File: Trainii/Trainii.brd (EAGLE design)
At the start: 50.8 x 71.1 mm, 32 parts, among them J1 APDS-9960, J2 Left Motor Encoder, J3 Right Motor Encoder, J4 Line Sensor 1, J5 Line Sensor 2, J6 Ultrasonic, J7 Left Motor Output, J8 Right Motor Output, J9 Lift Motor Output, U1 TPS61222DCKR, U2 BSS138

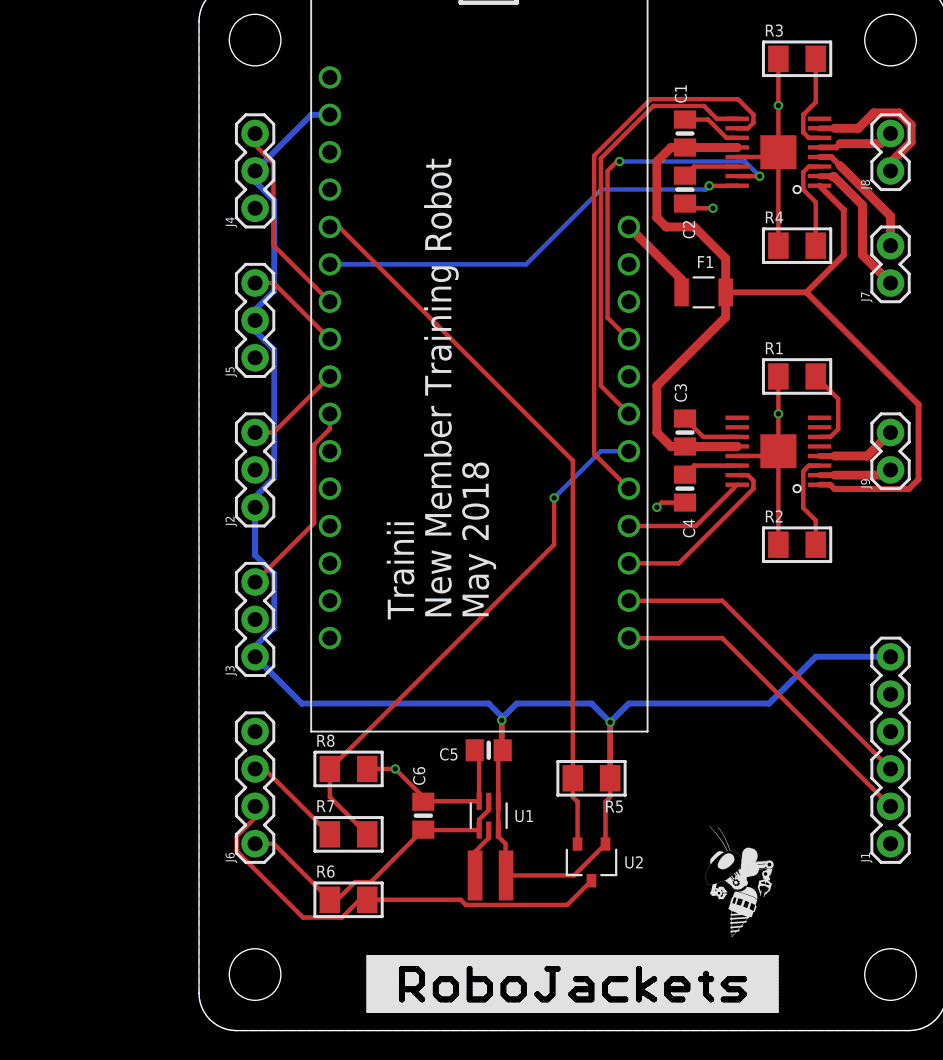
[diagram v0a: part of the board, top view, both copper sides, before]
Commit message: Updated Library, began fixing schematic
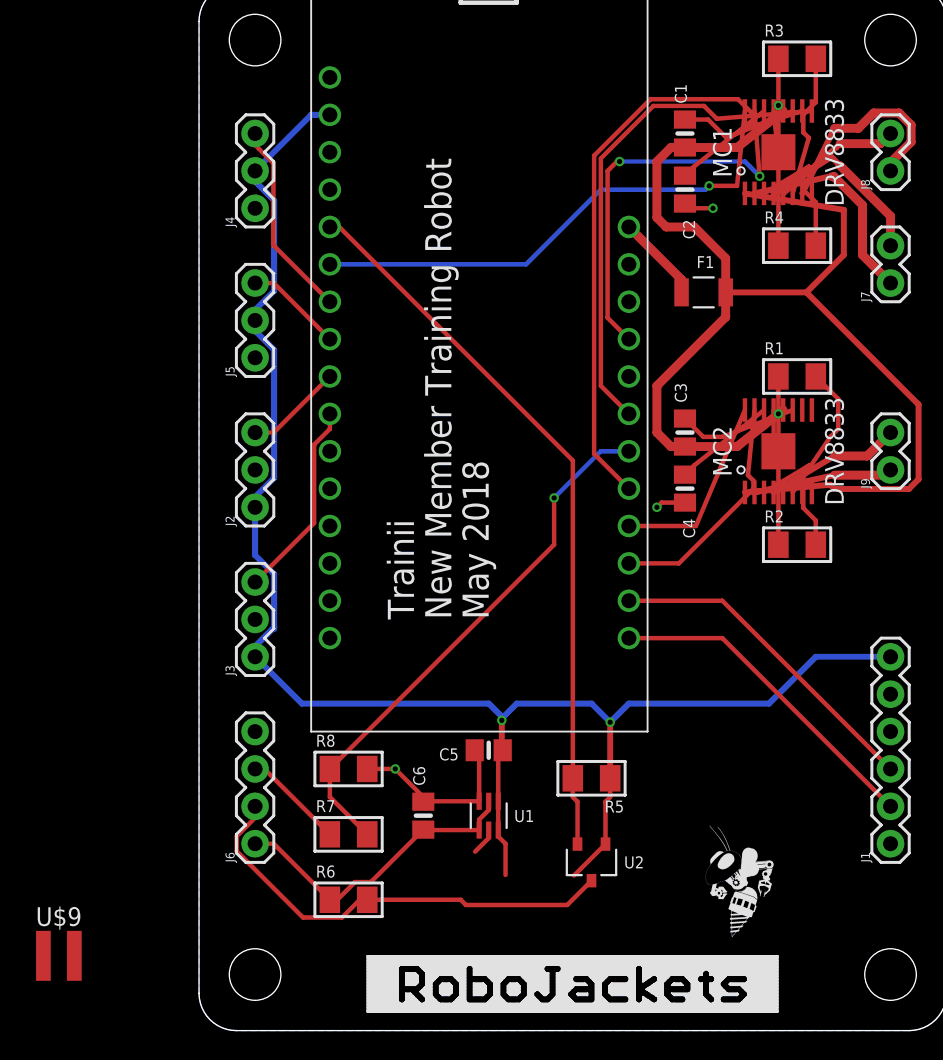
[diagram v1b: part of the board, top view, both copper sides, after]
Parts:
- removed U$12: VLS3012HBX, Trainii:VLS3012HBX
- added U$9: VLS3012HBX, Trainii:VLS3012HBX
- MC1, MC2: device Trainii:DRV8833 -> Trainii:HTSSOP-16
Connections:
- net 3V: now also U$9.1; no longer U$12.P$2
- net GND: now also MC1.13, MC1.17, MC2.13, MC2.17; no longer MC1.GND, MC1.GNDP, MC2.GND, MC2.GNDP
- net LEFT_0: now also MC1.2; no longer MC1.AOUT1
- net LEFT_1: now also MC1.4; no longer MC1.AOUT2
- net LEFT_A: now also MC1.16; no longer MC1.AIN1
- net LEFT_B: now also MC1.15; no longer MC1.AIN2
- net LIFT_0: now also MC2.2; no longer MC2.AOUT1
- net LIFT_1: now also MC2.4; no longer MC2.AOUT2
- net LIFT_A: now also MC2.16; no longer MC2.AIN1
- net LIFT_B: now also MC2.15; no longer MC2.AIN2
- net N$1: now also U$9.2; no longer U$12.P$1
- net N$10: now also MC1.3; no longer MC1.AISEN
- net N$3: now also MC2.11; no longer MC2.VCP
- net N$4: now also MC2.6; no longer MC2.BISEN
- net N$5: now also MC2.14; no longer MC2.VINT
- net N$6: now also MC2.3; no longer MC2.AISEN
- net N$7: now also MC1.11; no longer MC1.VCP
- net N$8: now also MC1.14; no longer MC1.VINT
- net N$9: now also MC1.6; no longer MC1.BISEN
- net RIGHT_0: now also MC1.7; no longer MC1.BOUT1
- net RIGHT_1: now also MC1.5; no longer MC1.BOUT2
- net RIGHT_A: now also MC1.9; no longer MC1.BIN1
- net RIGHT_B: now also MC1.10; no longer MC1.BIN2
- net VBAT_FUSE: now also MC1.1, MC1.12, MC2.1, MC2.12; no longer MC1.NSLEEP, MC1.VM, MC2.NSLEEP, MC2.VM
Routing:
- net VBAT_FUSE: track 72.6 -> 90.1 mm
- net LEFT_A: track 29.9 -> 35.0 mm
- net RIGHT_A: track 29.2 -> 34.3 mm
- net 3V: track 118.1 -> 113.4 mm
- net LIFT_A: track 8.52 -> 13.1 mm
- net LEFT_0: track 9.82 -> 14.4 mm
- net LIFT_0: track 4.97 -> 9.52 mm
- net N$7: track 4.07 -> 8.20 mm
- net N$3: track 4.07 -> 8.18 mm
- net RIGHT_0: track 10.7 -> 14.6 mm
- net LEFT_1: track 8.49 -> 12.3 mm
- net N$4: track 5.69 -> 9.52 mm
- net LIFT_1: track 5.48 -> 9.29 mm
- net LIFT_B: track 12.4 -> 16.1 mm
- net RIGHT_1: track 5.21 -> 8.85 mm
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
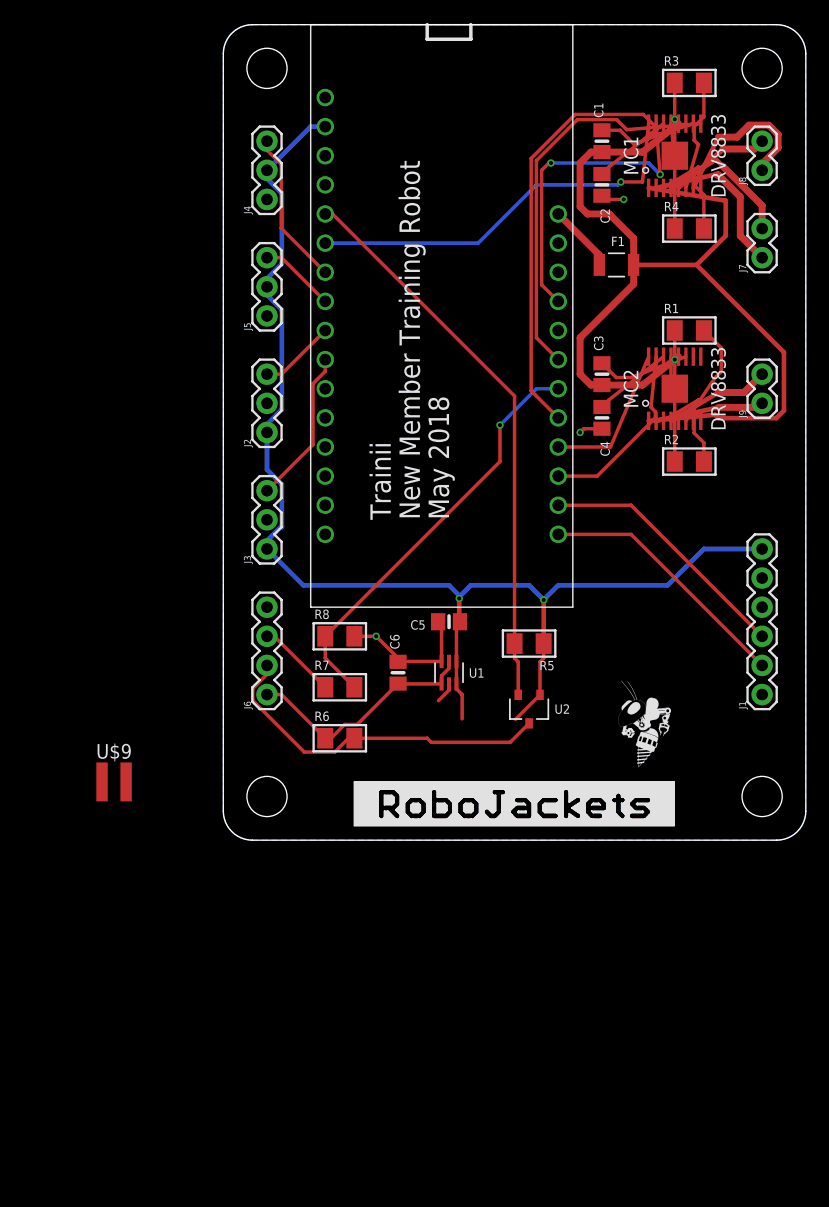
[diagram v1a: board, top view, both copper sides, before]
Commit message: Continued library update and finished schematic driver correction
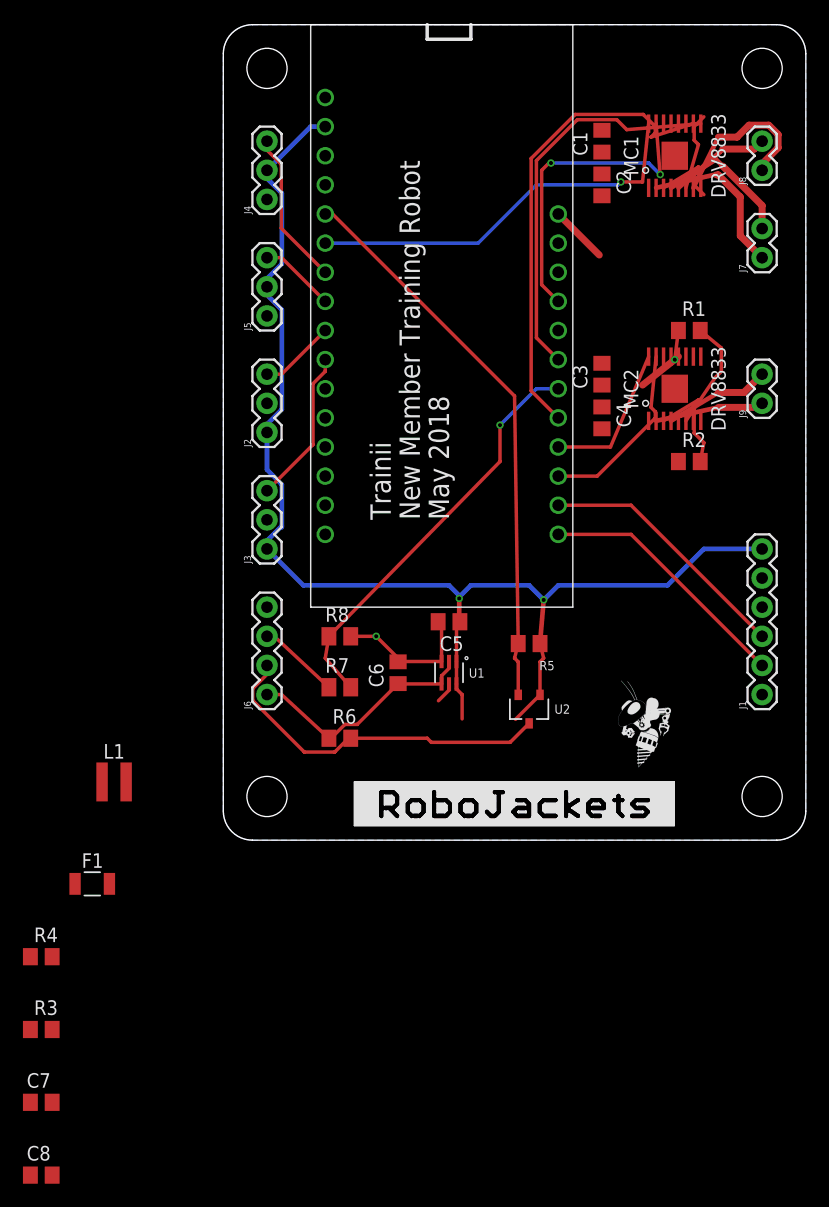
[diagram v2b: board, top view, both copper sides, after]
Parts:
- added C7, C8: 2.2uF, rcl:C0805
- C1, C3: value 0.1uF -> 0.01uF; device microbuilder:0805-NO -> rcl:C0805
- C2, C4: value 10µF -> 10uF; device microbuilder:0805-NO -> rcl:C0805
- C5: value 10uF -> 10uF 6.3V; device microbuilder:0805-NO -> rcl:C0805
- C6: value 10uF -> 10uF 16V; device microbuilder:0805-NO -> rcl:C0805
- F1: device Trainii:0ZCJ -> Trainii:1206
- L1: value VLS3012HBX -> 4.7 uH
- R1, R2, R5, R6: device microbuilder:_1206 -> rcl:R0805
- R3, R4: value 0.2Ω -> 0.2 Ohm; device microbuilder:_1206 -> rcl:R0805
- R7, R8: device microbuilder:_1206 -> rcl:M0805
- moved R3 100.0 mm to (-15.9, -16.5)
- moved R4 85.0 mm to (-15.9, -10.2)
- moved F1 70.7 mm to (-11.4, -3.81)
- renumbered U$9 to L1
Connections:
- removed net N$3: C3.2, MC2.11
- new net MOTOR_FAULT: MC1.8, MC2.8, U$6.21
- new net N$11: C3.1, MC2.11
- new net N$2: R1.1, R2.1
- net GND: now also C7.2, C8.2, R3.2, R4.2; no longer R1.1, R2.1, R3.1, R4.1
- net N$10: now also R4.1; no longer R4.2
- net N$5: now also C8.1; no longer C4.1
- net N$7: now also C1.1; no longer C1.2
- net N$8: now also C7.1; no longer C2.1
- net N$9: now also R3.1; no longer R3.2
- net VBAT_FUSE: now also C1.2, C2.1, C3.2, C4.1; no longer C1.1, C3.1, F1.2
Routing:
- net VBAT_FUSE: track 90.1 -> 3.99 mm
- net GND: track 47.6 -> 12.6 mm, vias 5 -> 1
- net N$7: track 8.20 -> 0.00 mm
- net N$3: track 8.18 -> 0.00 mm
- net N$8: track 6.94 -> 0.00 mm
- net N$5: track 6.94 -> 0.00 mm
- net N$9: track 9.81 -> 6.86 mm
- net N$10: track 9.43 -> 6.47 mm
- net N$2: track 0.00 -> 2.56 mm, vias 0 -> 1
- net VBAT: track 5.93 -> 5.06 mm

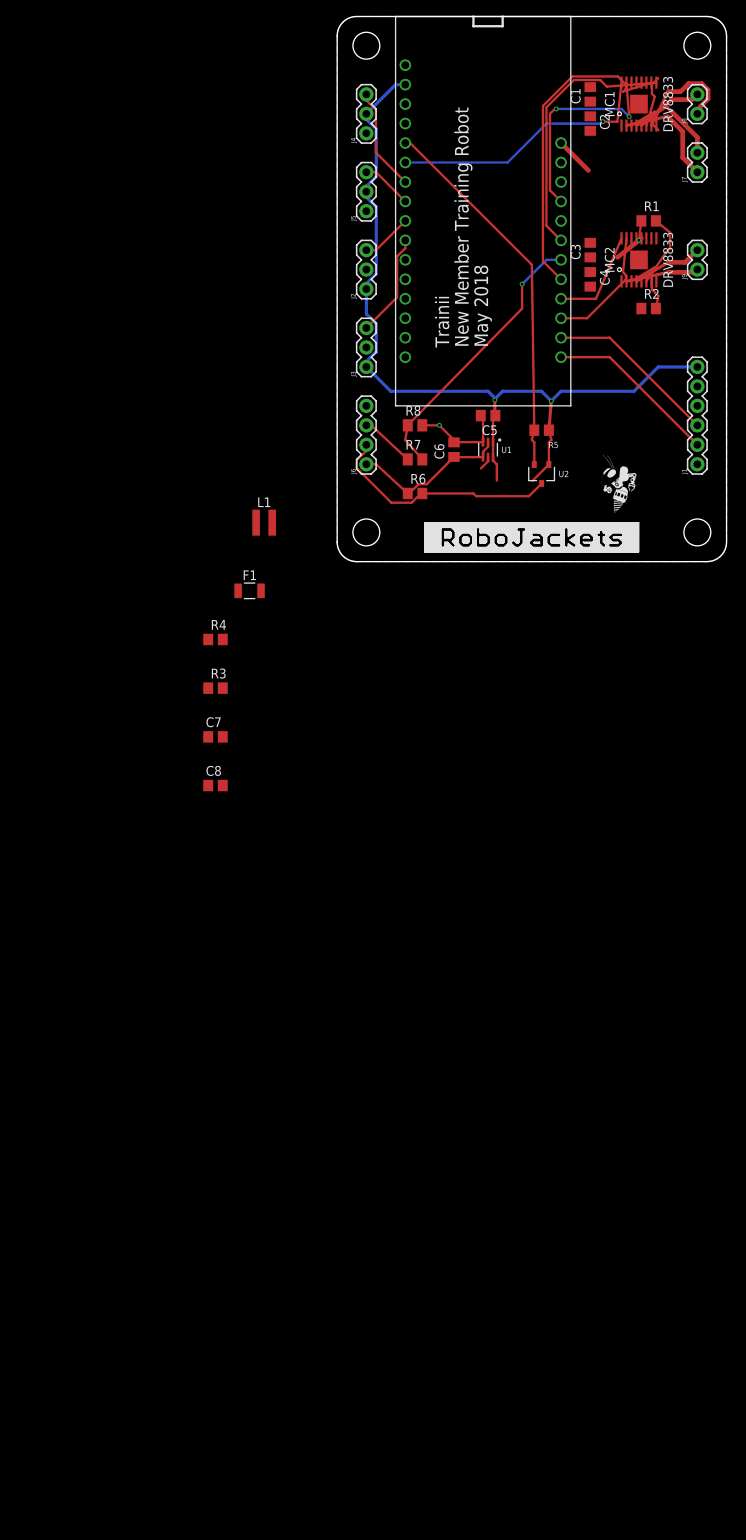
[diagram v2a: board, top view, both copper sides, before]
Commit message: Added new battery connector
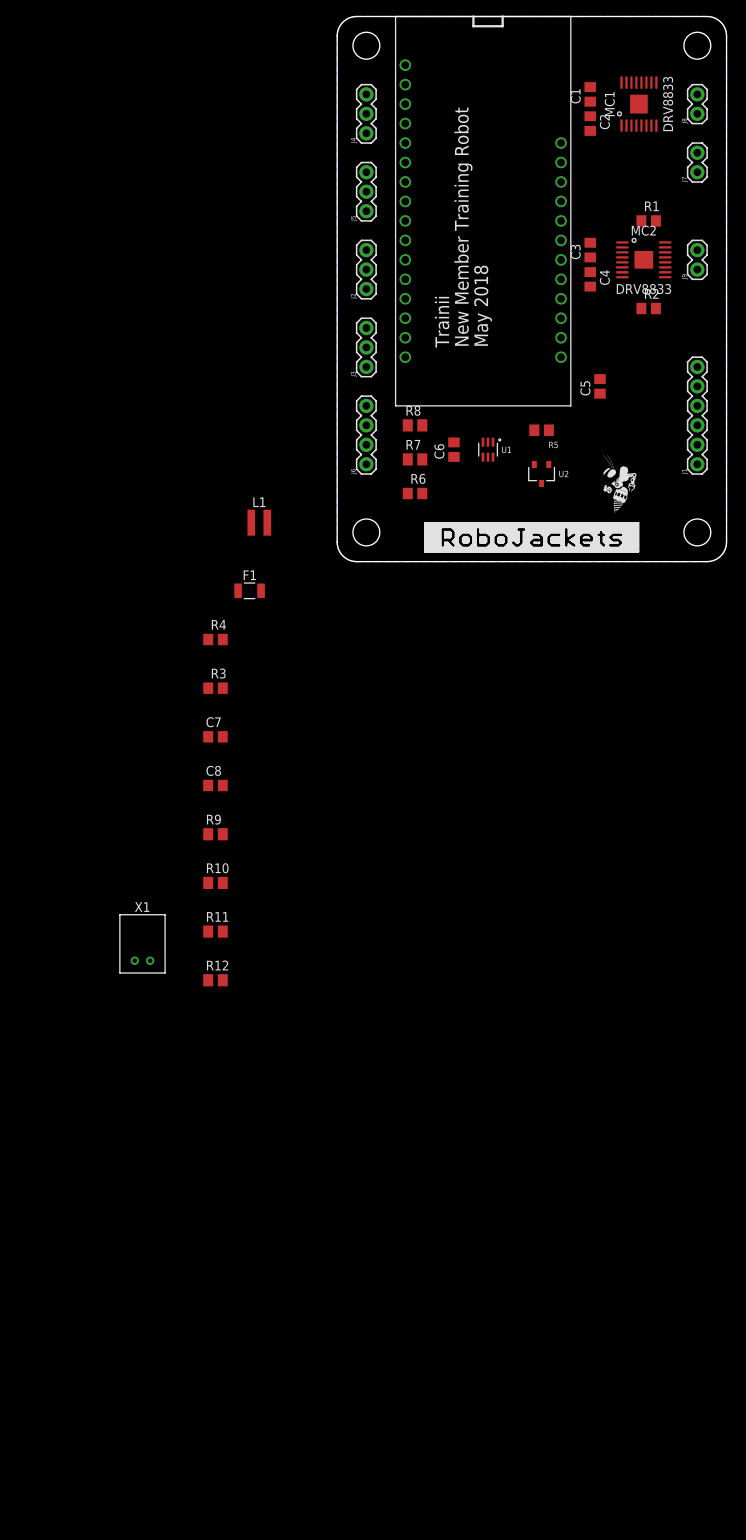
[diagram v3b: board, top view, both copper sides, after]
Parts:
- added R10, R12: 91Ω, rcl:M0805
- added R11, R9: 47Ω, rcl:M0805
- added X1: JST-PH2, Trainii:JST-PH
- moved C5 15.1 mm to (34.3, 22.9), turned to 90 degrees
- moved MC2 0.64 mm to (40.0, 39.4), turned to 0 degrees
- moved L1 0.63 mm to (-10.2, 5.08)
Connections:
- net ECHO renamed ECHO_5V
- net ECHO3.3 renamed ECHO_3V3
- net TRIG renamed TRIG_5V
- net TRIG3.3 renamed TRIG_3V3
- removed net 3V: C5.1, J1.6, J2.1, J3.1, J4.2, J5.2, L1.1, R5.1, U$6.3V, U1.1, U1.6, U2.1
- new net 3V3: C5.1, J1.6, J2.1, J3.1, L1.1, R5.1, U$6.3V, U1.1, U1.6, U2.1
- new net LINE_OUT_1_3V3: R10.1, R9.2
- new net LINE_OUT_1_5V: J4.3, R9.1
- new net LINE_OUT_2_3V3: R11.2, R12.1
- new net LINE_OUT_2_5V: J5.3, R11.1
- net +5V: now also J4.2, J5.2
- net GND: now also R10.2, R12.2, X1.1
- net LINE_OUT_1: no longer J4.3
- net LINE_OUT_2: no longer J5.3
- net VBAT: now also X1.2
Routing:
- net 3V: track 113.4 -> 0.00 mm, vias 2 -> 0
- net TRIG_3V3: track 49.3 -> 0.00 mm
- net RIGHT_B: track 41.4 -> 0.00 mm
- net ECHO_3V3: track 36.2 -> 0.00 mm, vias 1 -> 0
- net LEFT_A: track 35.0 -> 0.00 mm, vias 1 -> 0
- net RIGHT_A: track 34.3 -> 0.00 mm
- net TRIG_5V: track 30.9 -> 0.00 mm
- net LEFT_B: track 27.5 -> 0.00 mm, vias 2 -> 0
- net SDA: track 22.5 -> 0.00 mm
- net SCL: track 22.5 -> 0.00 mm
- net +5V: track 20.9 -> 0.00 mm
- net LIFT_B: track 16.1 -> 0.00 mm
- net RIGHT_0: track 14.6 -> 0.00 mm
- net LEFT_0: track 14.4 -> 0.00 mm
- net LINE_OUT_1: track 13.5 -> 0.00 mm
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
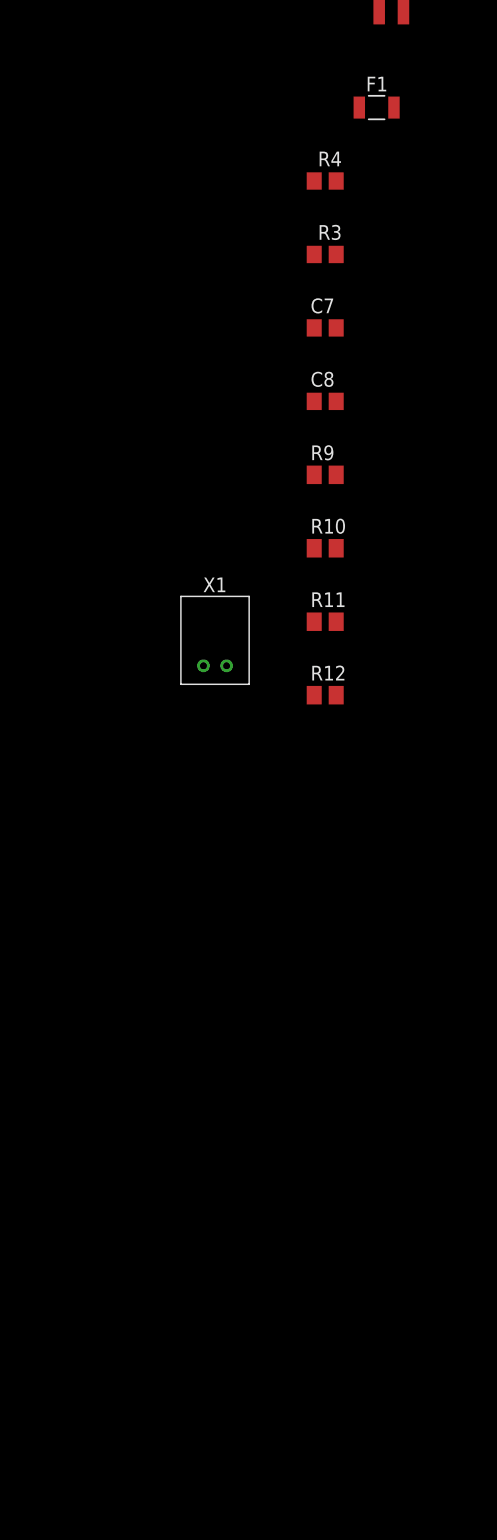
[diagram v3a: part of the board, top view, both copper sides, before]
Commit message: edited schematic to include 3-position switch to select charging, running, or off
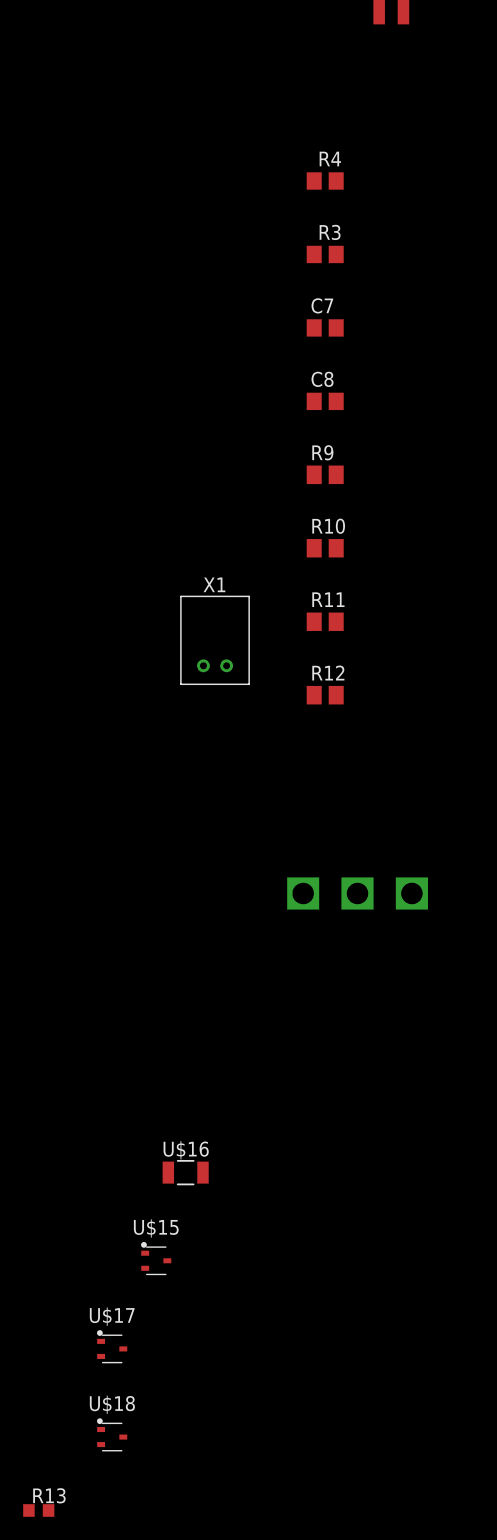
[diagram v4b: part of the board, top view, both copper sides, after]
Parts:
- removed F1: 0ZCJ0100FF2E, Trainii:1206
- added R13: (no value), rcl:R0603
- added U$14: 100SP3T, Trainii:100SP3T
- added U$15, U$17, U$18: MCH3383SC-70FL, Trainii:SOTFL65P210X90-3
- added U$16: 0ZCJ0100FF2E, Trainii:1206
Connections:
- removed net VBAT_FUSE: C1.2, C2.1, C3.2, C4.1, MC1.1, MC1.12, MC2.1, MC2.12
- new net N$13: R13.2, U$14.P$3, U$17.1, U$18.1, U$18.3
- new net N$3: U$14.P$1, U$15.1, U$18.2
- new net VBAT_H: U$15.2, U$6.BAT
- new net VBAT_MOTOR: C1.2, C2.1, C3.2, C4.1, MC1.1, MC1.12, MC2.1, MC2.12, U$17.2
- net GND: now also R13.1
- net VBAT: now also U$14.P$2, U$15.3, U$16.1, U$16.2, U$17.3; no longer F1.1, U$6.BAT
